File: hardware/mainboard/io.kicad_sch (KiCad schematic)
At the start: 44 parts, among them J2 MINI_DP_SINK, J3 DEBUG, J4 USB_C_Receptacle, Q10 BSS138, U12 TPD4E02B04DQA, U13 TPD4E02B04DQA, U14 CBTL02043A, U15 FUSB302B11MPX, U16 USB3318, X1 831056169

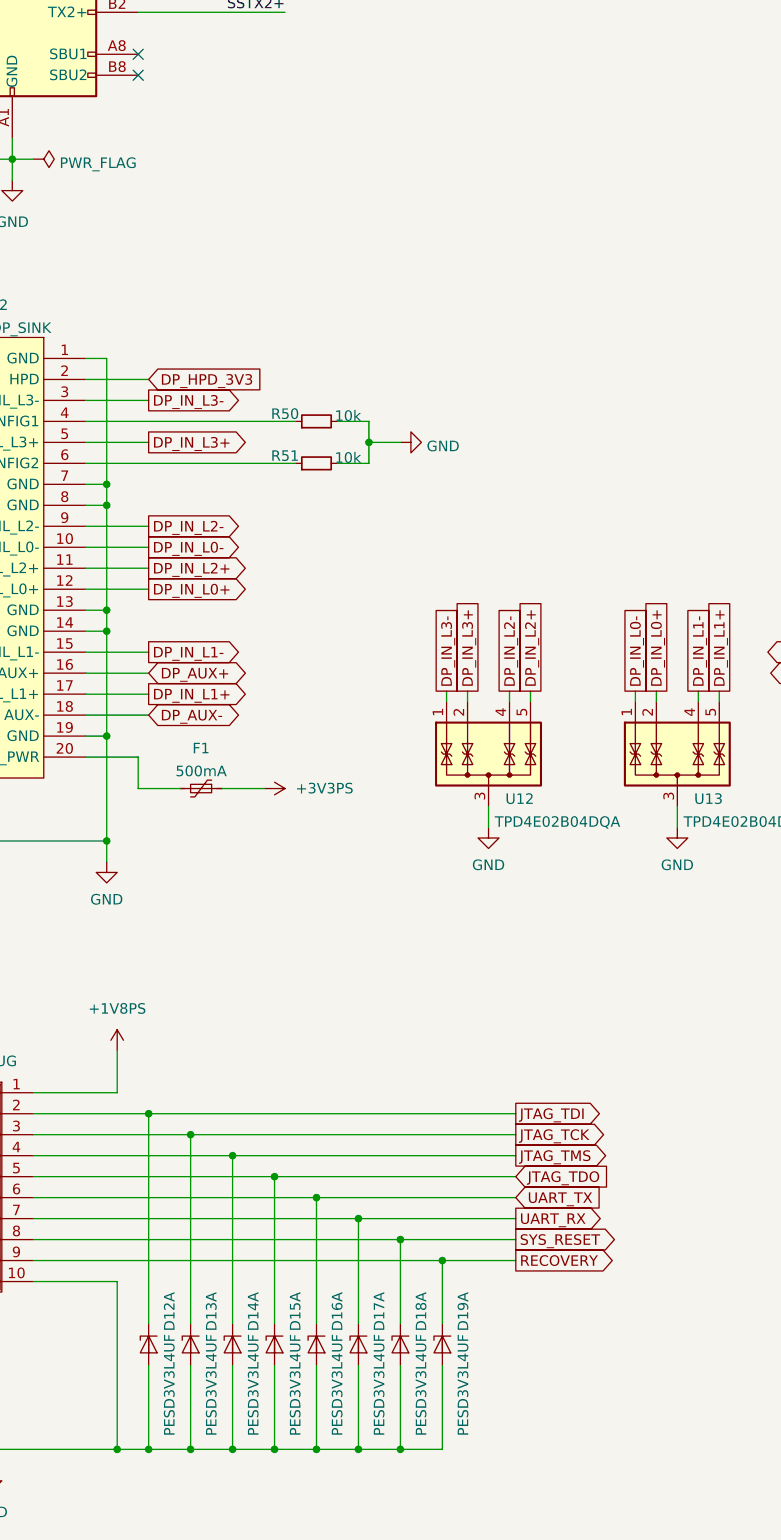
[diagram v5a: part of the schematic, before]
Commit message: Rework power arch to add 3V3PL; 5x PL RGB LEDs
Signed-off-by: gatecat <gatecat@ds0.me>
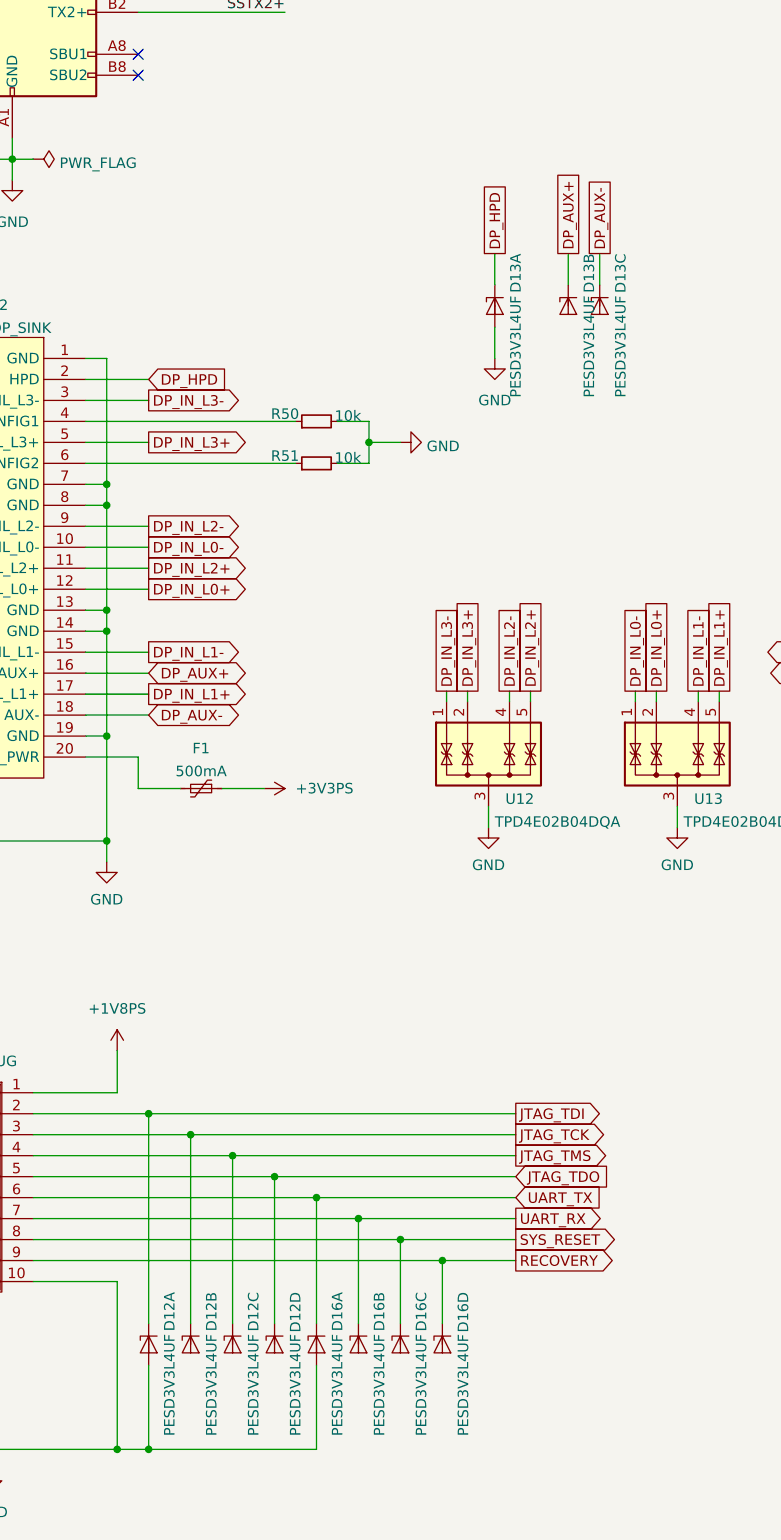
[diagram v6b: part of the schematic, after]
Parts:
- added D13: PESD3V3L4UF, Package_TO_SOT_SMD:SOT-886, symbol Power_Protection:PESD3V3L4UF
- renumbered D15 to D12, D13 to D12, D14 to D12, D18 to D16, D17 to D16, D19 to D16
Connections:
- net DP_AUX+: now also D13.3 (K2)
- net DP_AUX-: now also D13.4 (K3)
- net GND: now also D13.2 (A), D13.5 (A); no longer D12.2 (A), D12.2 (A), D12.2 (A), D12.5 (A), D12.5 (A), D12.5 (A), D16.2 (A), D16.2 (A), D16.2 (A), D16.5 (A), D16.5 (A), D16.5 (A)
- net JTAG_TCK: now also D12.3 (K2); no longer D12.1 (K1)
- net JTAG_TDO: now also D12.6 (K4); no longer D12.1 (K1)
- net JTAG_TMS: now also D12.4 (K3); no longer D12.1 (K1)
- net RECOVERY: now also D16.6 (K4); no longer D16.1 (K1)
- net SYS_RESET: now also D16.4 (K3); no longer D16.1 (K1)
- net UART_RX: now also D16.3 (K2); no longer D16.1 (K1)
- net DP_HPD_3V3 renamed DP_HPD
- net DP_HPD: now also D13.1 (K1)

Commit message: Footprint assignment updates
Signed-off-by: gatecat <gatecat@ds0.me>
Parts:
- J2: footprint (none) -> meowality:E9320-001-01
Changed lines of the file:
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@@
     (property "Reference" "J2" (id 0) (at 45.6819 121.8143 0))
     (property "Value" "MINI_DP_SINK" (id 1) (at 45.6819 124.5894 0))
-    (property "Footprint" "" (id 2) (at 43.18 177.8 0)
+    (property "Footprint" "meowality:E9320-001-01" (id 2) (at 43.18 177.8 0)
       (effects (font (size 1.27 1.27)) hide)
     )

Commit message: All parts placed
Signed-off-by: gatecat <gatecat@ds0.me>
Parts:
- R52, R53: value 5.1k -> DNP
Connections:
- net SSTX1+: now also C54.1
- net SSTX1-: now also C55.1
- net SSTX2+: now also C56.1
- net SSTX2-: now also C57.1
- net SSTXC1+: no longer C54.1
- net SSTXC1-: no longer C55.1
- net SSTXC2+: no longer C56.1
- net SSTXC2-: no longer C57.1
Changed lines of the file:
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@@
     (effects (font (size 1.27 1.27)) (justify left bottom))
   )
-  (label "SSTXC2+" (at 113.03 71.12 0)
+  (label "SSTX2+" (at 113.03 71.12 0)
     (effects (font (size 1.27 1.27)) (justify left bottom))
   )
@@
     (effects (font (size 1.27 1.27)) (justify right bottom))
   )
-  (label "SSTXC1-" (at 113.03 63.5 0)
+  (label "SSTX1-" (at 113.03 63.5 0)
     (effects (font (size 1.27 1.27)) (justify left bottom))
   )
@@
     (effects (font (size 1.27 1.27)) (justify right bottom))
   )
-  (label "SSTXC2-" (at 113.03 73.66 0)
+  (label "SSTX2-" (at 113.03 73.66 0)
     (effects (font (size 1.27 1.27)) (justify left bottom))
   )
@@
     (effects (font (size 1.27 1.27)) (justify left bottom))
   )
-  (label "SSTXC1+" (at 113.03 60.96 0)
+  (label "SSTX1+" (at 113.03 60.96 0)
     (effects (font (size 1.27 1.27)) (justify left bottom))
   )
@@
     (in_bom yes) (on_board yes)
     (property "Reference" "R53" (id 0) (at 85.09 48.26 90))
-    (property "Value" "5.1k" (id 1) (at 85.09 45.72 90))
+    (property "Value" "DNP" (id 1) (at 85.09 45.72 90))
     (property "Footprint" "Resistor_SMD:R_0402_1005Metric" (id 2) (at 85.09 43.18 0)
       (effects (font (size 1.27 1.27)) hide)
@@
   (symbol (lib_id "Device:R_Small") (at 85.09 40.64 90) (unit 1)
     (in_bom yes) (on_board yes) (fields_autoplaced)
-    (property "Reference" "R52" (id 0) (at 85.09 35.9369 90))
-    (property "Value" "5.1k" (id 1) (at 85.09 38.712 90))
+    (property "Reference" "R52" (id 0) (at 85.09 34.29 90))
+    (property "Value" "DNP" (id 1) (at 85.09 36.83 90))
     (property "Footprint" "Resistor_SMD:R_0402_1005Metric" (id 2) (at 85.09 40.64 0)
       (effects (font (size 1.27 1.27)) hide)
